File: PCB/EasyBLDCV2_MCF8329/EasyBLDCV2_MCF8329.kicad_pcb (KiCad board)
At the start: 4 copper layers, 72.4 x 45.7 mm, 72 parts, among them J1 10159560-A00221RLF, Q1 CSD17573Q5B, Q2 CSD17573Q5B, Q3 CSD17573Q5B, Q4 CSD17573Q5B, Q5 CSD17573Q5B, Q6 CSD17573Q5B, U1 MCF8329A1IREER

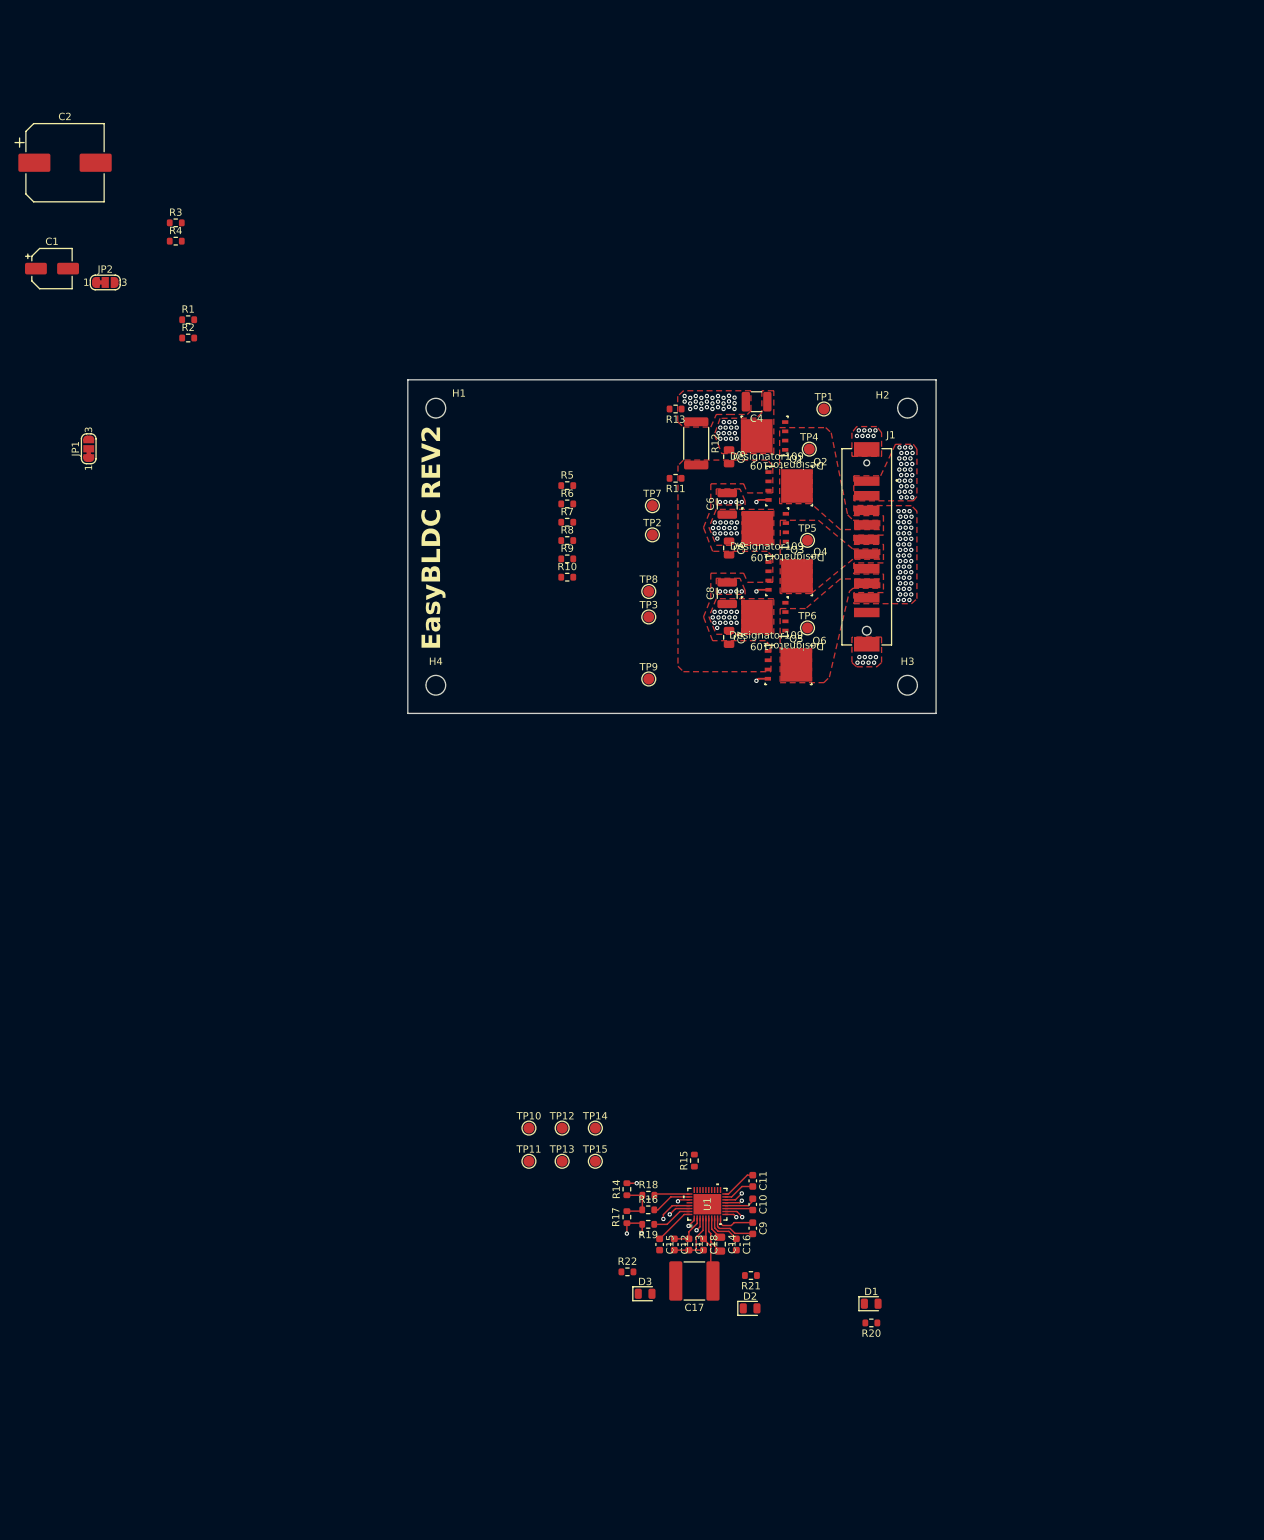
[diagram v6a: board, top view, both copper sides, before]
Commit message: Finished Silscreen
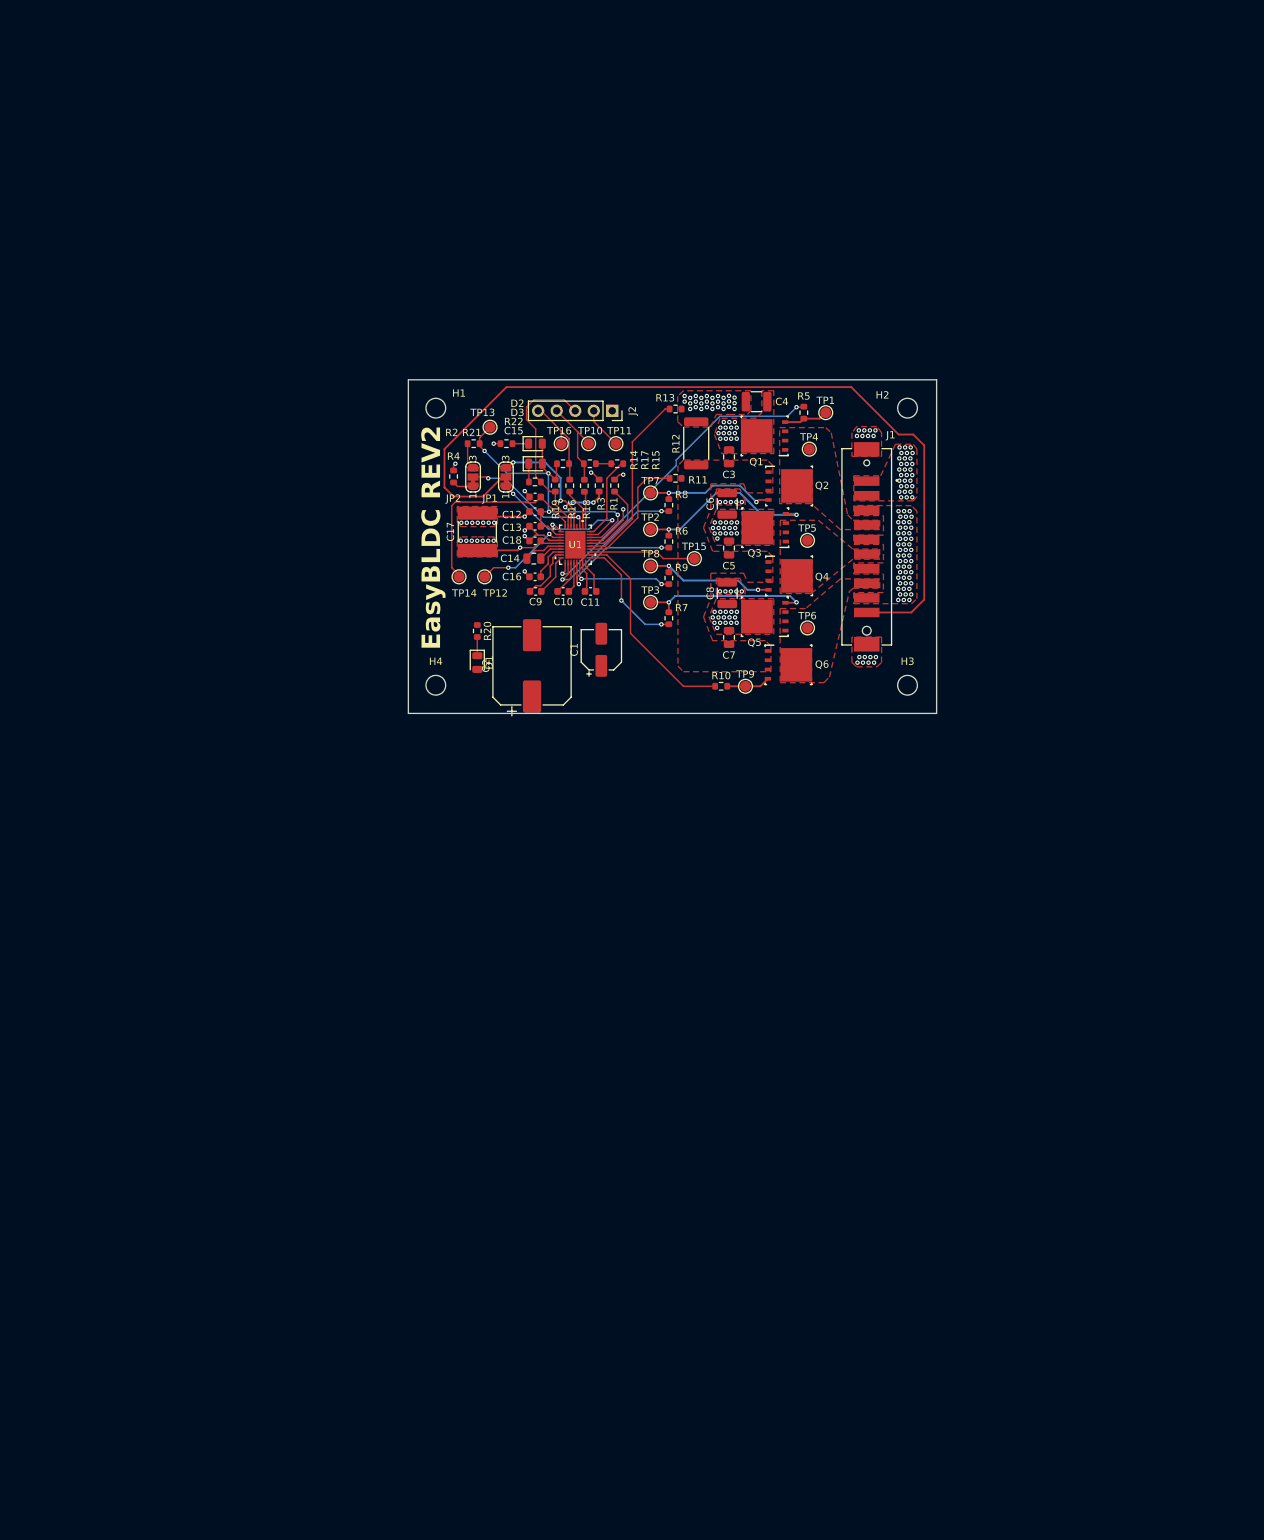
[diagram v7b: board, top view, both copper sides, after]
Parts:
- added J2: Conn_01x05_Pin, Connector_PinSocket_2.54mm:PinSocket_1x05_P2.54mm_Vertical, F.Cu at (52.2, 32.8)
- added TP16: TestPoint, TestPoint:TestPoint_Pad_D1.5mm, F.Cu at (45.2, 37.2)
- moved D2 122.1 mm to (41.7, 37.2)
- moved R21 118.8 mm to (37.8, 37.2), turned to 0 degrees
- moved D3 114.7 mm to (41.7, 40.0)
- moved R20 109.1 mm to (33.8, 62.9), turned to -90 degrees
- moved R22 109.0 mm to (41.6, 42.5), turned to 180 degrees
- moved C17 106.9 mm to (33.8, 49.3), turned to 90 degrees
- moved C15 103.8 mm to (41.7, 44.6), turned to 180 degrees
- moved R17 103.4 mm to (49.2, 40.0), turned to 0 degrees
- moved D1 103.1 mm to (33.8, 67.2), turned to -90 degrees
- moved C12 102.2 mm to (41.7, 46.6), turned to 180 degrees
- moved R19 102.0 mm to (44.4, 43.0), turned to 90 degrees
- moved TP13 101.1 mm to (35.5, 35.0)
- moved C13 100.7 mm to (41.7, 48.6), turned to 180 degrees
- moved R16 99.8 mm to (46.4, 43.0), turned to -90 degrees
- moved R14 99.8 mm to (45.5, 40.0), turned to 180 degrees
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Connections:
- J1 pad 10: COM -> INPUT
- R17 pad 1: MCX_SCL -> MCX_SDA
- R18 pad 1: MCX_SCL -> MCX_SDA
- TP10 pad 1: DACOUT/SOX/SPEED_ANA -> MCX_SDA
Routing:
- net INPUT: track 0.00 -> 117.6 mm
- net GH_A: track 1.67 -> 44.7 mm, vias 1 -> 2
- net AVDD: track 11.5 -> 51.5 mm, vias 3 -> 4
- net GL_C: track 0.00 -> 29.1 mm
- net Net-(Q3-G): track 0.00 -> 25.7 mm, vias 0 -> 2
- net SN: track 0.00 -> 24.9 mm
- net Net-(Q5-G): track 0.00 -> 23.6 mm, vias 0 -> 2
- net Net-(U1B-DVDD): track 5.48 -> 28.7 mm
- net nFAULT: track 5.56 -> 27.1 mm
- net SPEED/WAKE: track 0.00 -> 21.4 mm, vias 0 -> 2
- net GND: track 10.3 -> 31.0 mm, vias 107 -> 124
- net GL_A: track 2.67 -> 21.1 mm, vias 1 -> 2
- net FGOUT: track 0.00 -> 17.4 mm
- net SP: track 0.00 -> 17.4 mm
- net GH_C: track 0.00 -> 16.7 mm, vias 0 -> 2
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
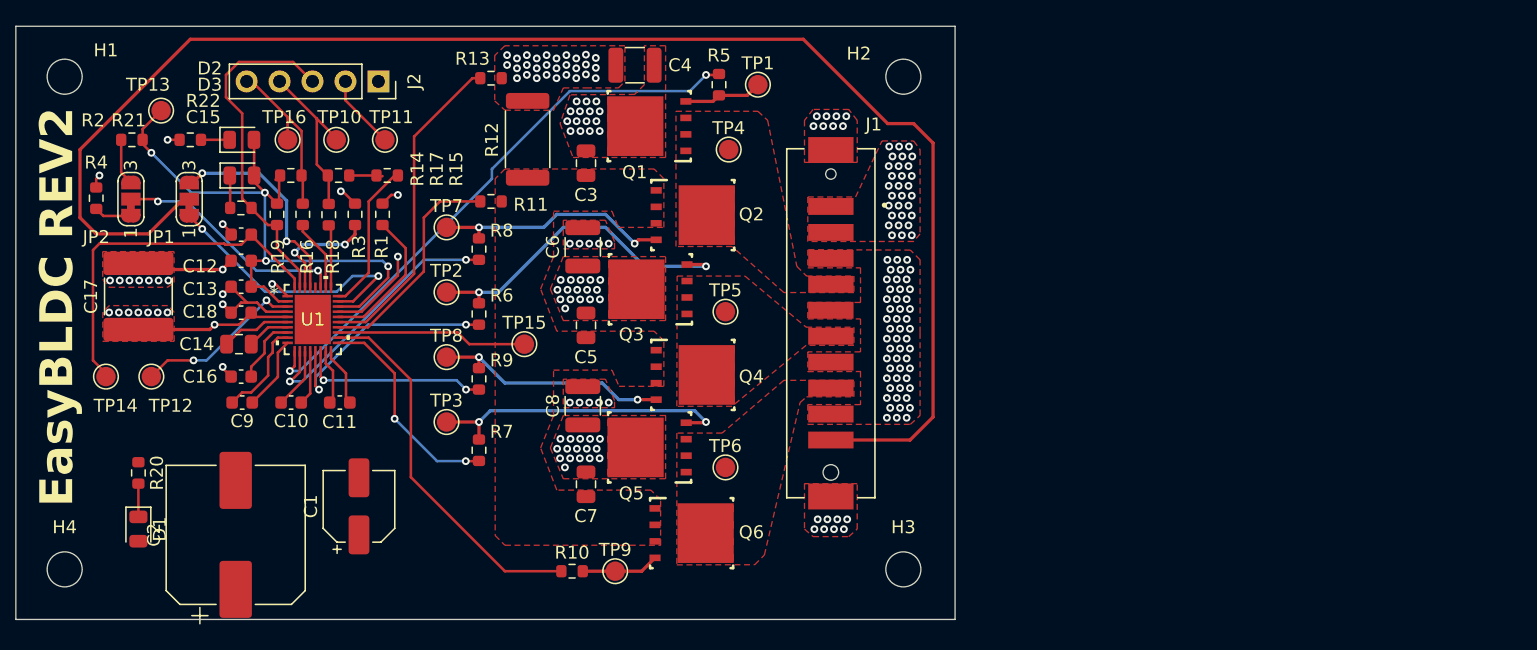
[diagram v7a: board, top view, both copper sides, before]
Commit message: Changed Stackup
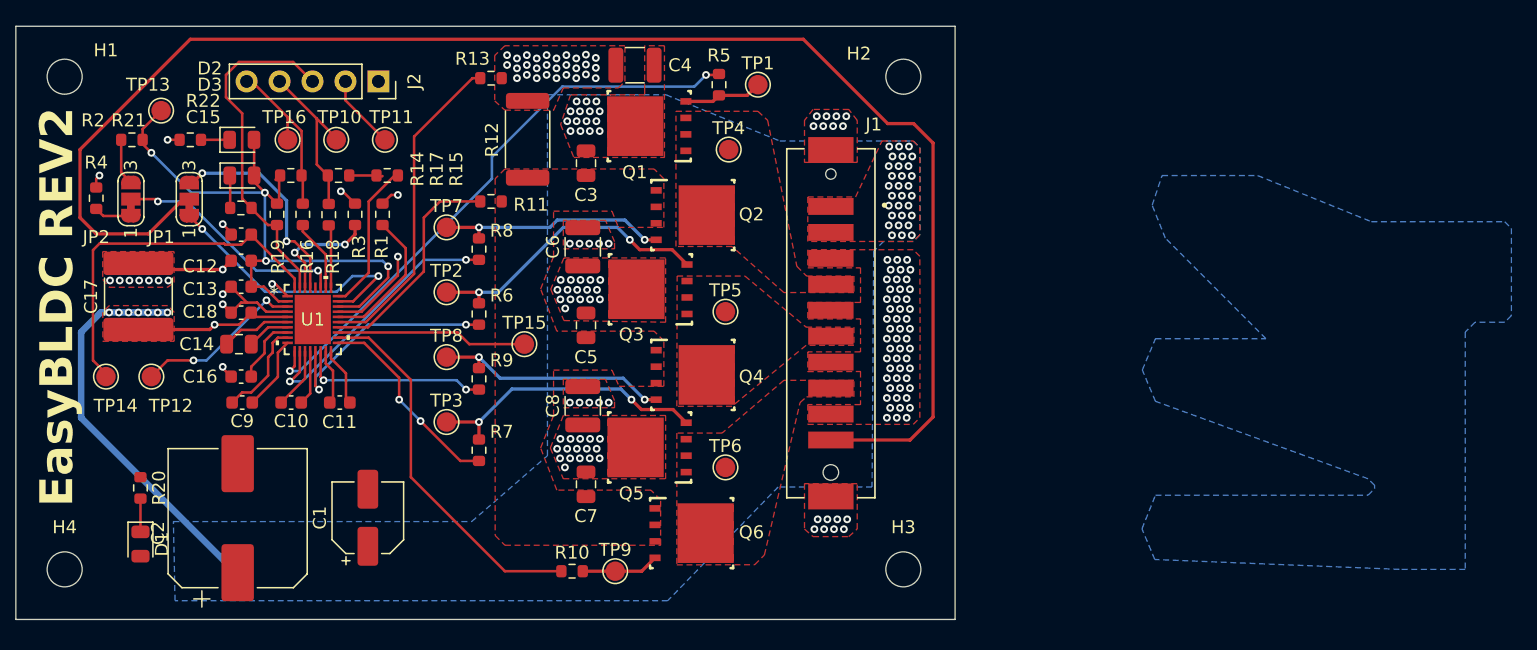
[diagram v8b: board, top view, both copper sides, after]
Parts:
- moved C2 1.30 mm to (41.4, 66.4)
- moved D1 1.17 mm to (33.9, 68.4)
- moved R20 1.17 mm to (33.9, 64.1)
- moved C1 1.12 mm to (51.4, 66.4)
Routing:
- net PVDD: track 11.1 -> 42.2 mm
- net Net-(Q3-G): track 25.7 -> 22.6 mm
- net Net-(Q5-G): track 23.6 -> 22.0 mm
- net GH_C: track 16.7 -> 15.6 mm
- net Net-(Q2-G): track 18.5 -> 17.9 mm
- net GH_A: track 44.7 -> 45.2 mm
- added copper zone on In1.Cu, net GND
- added copper zone on B.Cu, net PVDD
- removed copper zone on In1.Cu, net PVDD
